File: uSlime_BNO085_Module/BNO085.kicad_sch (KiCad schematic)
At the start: 12 parts, among them CN1 X1502WR-05K-N0SN, J1 Conn_01x05, U1 BNO085

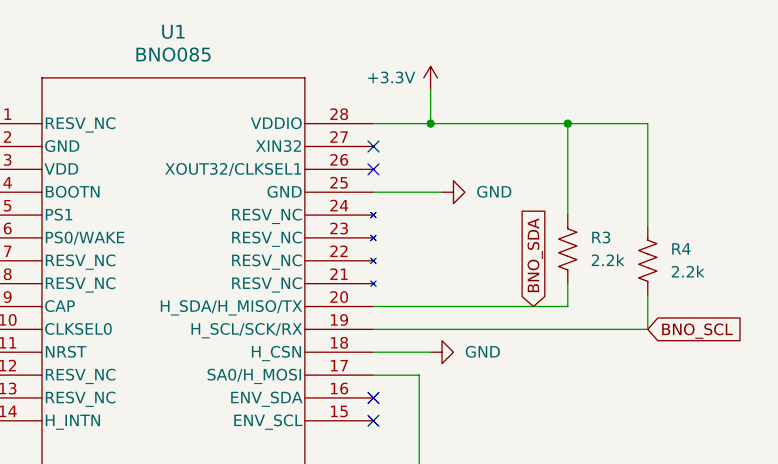
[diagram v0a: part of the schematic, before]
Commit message: Connect pin 26 to GND
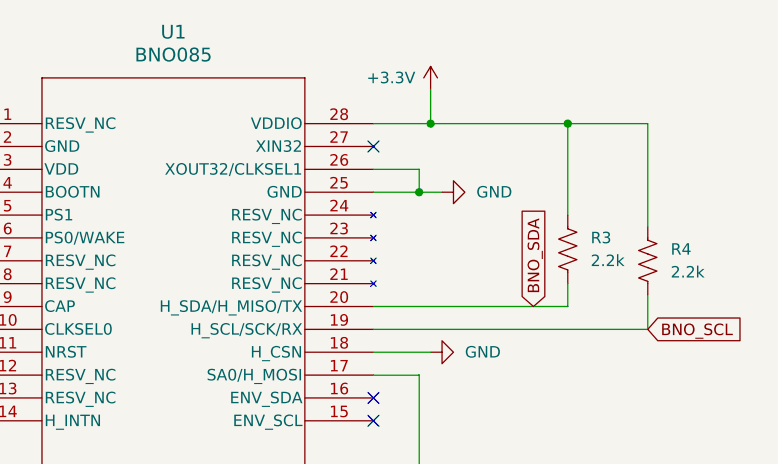
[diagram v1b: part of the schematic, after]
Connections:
- net GND: now also U1.26 (XOUT32/CLKSEL1)
- no-connect marks 4 -> 3
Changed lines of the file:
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@@
+	)
+	(junction
+		(at 162.56 69.85)
+		(diameter 0)
+		(color 0 0 0 0)
 	)
 	(junction
@@
 	)
 	(no_connect
-		(at 157.48 67.31)
-	)
-	(no_connect
 		(at 157.48 95.25)
 	)
@@
 	(wire
 		(pts
+			(xy 157.48 67.31) (xy 162.56 67.31)
+		)
+		(stroke
+			(width 0)
+			(type default)
+		)
+	)
+	(wire
+		(pts
 			(xy 92.71 59.69) (xy 92.71 67.31)
 		)
@@
 	(wire
 		(pts
-			(xy 165.1 69.85) (xy 157.48 69.85)
+			(xy 165.1 69.85) (xy 162.56 69.85)
 		)
 		(stroke
@@
 	(wire
 		(pts
+			(xy 162.56 67.31) (xy 162.56 69.85)
+		)
+		(stroke
+			(width 0)
+			(type default)
+		)
+	)
+	(wire
+		(pts
 			(xy 113.03 74.93) (xy 107.95 74.93)
 		)
@@
 		)
 		(stroke
+			(width 0)
+			(type default)
+		)
+	)
+	(wire
+		(pts
+			(xy 162.56 69.85) (xy 157.48 69.85)
+		)
+		(stroke

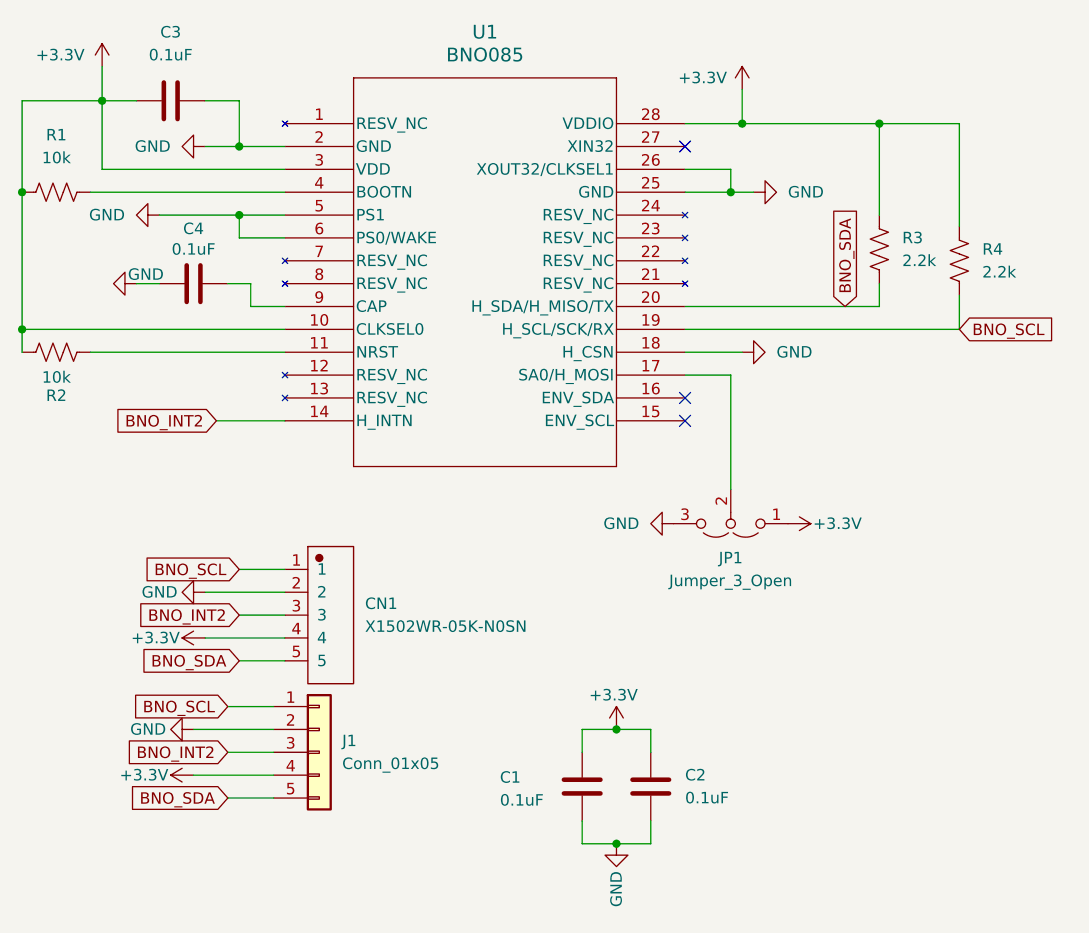
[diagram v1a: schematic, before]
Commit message: Modify PCB to add resistors to pins 14, 15, 16
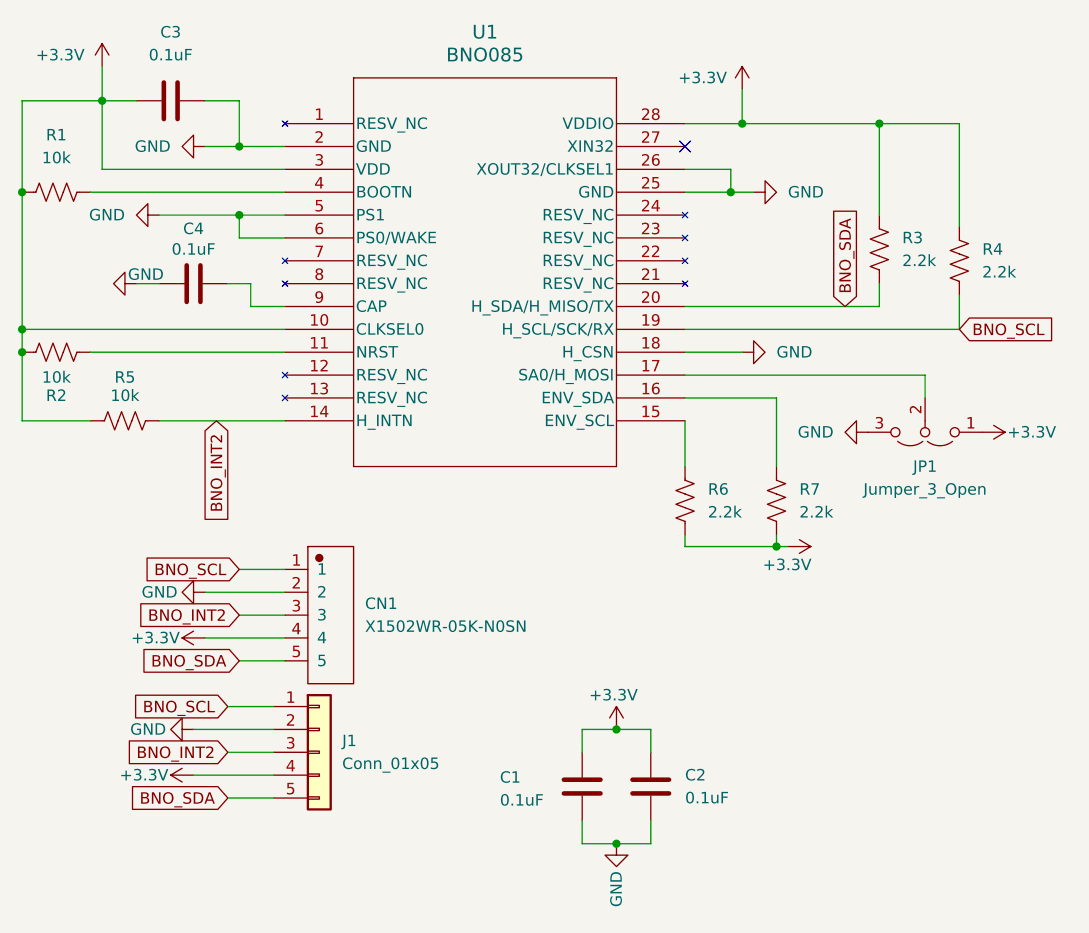
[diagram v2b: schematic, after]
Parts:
- added R5: 10k, Resistor_SMD:R_0402_1005Metric, symbol uSlime:R_US
- added R6, R7: 2.2k, Resistor_SMD:R_0402_1005Metric, symbol uSlime:R_US
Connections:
- net +3.3V: now also R5.1, R6.2, R7.2
- net BNO_INT2: now also R5.2
- net at U1.15 (ENV_SCL): now also R6.1
- net at U1.16 (ENV_SDA): now also R7.1
- no-connect marks 3 -> 1
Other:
- moved on the sheet: JP1
